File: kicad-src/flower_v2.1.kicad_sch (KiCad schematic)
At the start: 24 parts, among them J1 Conn_01x05_Male, J2 Capacitance PCB sensor, Q1 BSS84, SW1 SW_Push, SW2 SW_Push, U1 E18-MS1-PCB, U2 HSU-CHM-01A, U3 DS18B20U

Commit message: Update PCB layout
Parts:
- gave numbers to parts that had none: 1
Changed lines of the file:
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@@
   (symbol (lib_id "Device:C") (at 242.57 137.16 0) (unit 1)
     (in_bom yes) (on_board yes) (fields_autoplaced)
-    (property "Reference" "C?" (id 0) (at 246.38 135.8899 0)
+    (property "Reference" "C6" (id 0) (at 246.38 135.8899 0)
       (effects (font (size 1.27 1.27)) (justify left))
     )
@@
   (symbol (lib_id "Graphic:Logo_Open_Hardware_Small") (at 276.86 175.26 0) (unit 1)
     (in_bom yes) (on_board yes) (fields_autoplaced)
-    (property "Reference" "#LOGO?" (id 0) (at 276.86 168.275 0)
+    (property "Reference" "#LOGO1" (id 0) (at 276.86 168.275 0)
       (effects (font (size 1.27 1.27)) hide)
     )
@@
   (symbol_instances
     (path "/13f92a83-1550-43ad-ac23-b0e99ea3e589"
-      (reference "#LOGO?") (unit 1) (value "Logo_Open_Hardware_Small") (footprint "")
+      (reference "#LOGO1") (unit 1) (value "Logo_Open_Hardware_Small") (footprint "")
     )
     (path "/2f47706e-deb1-47a3-ad7d-bf0831227ea1"
@@
     )
     (path "/1078c351-8d03-4a20-b476-db003f88e220"
-      (reference "C?") (unit 1) (value "100nF") (footprint "Capacitor_SMD:C_0402_1005Metric")
+      (reference "C6") (unit 1) (value "100nF") (footprint "Capacitor_SMD:C_0402_1005Metric")
     )
     (path "/fd96ccba-4af7-423d-a91a-5897f7f71caa"

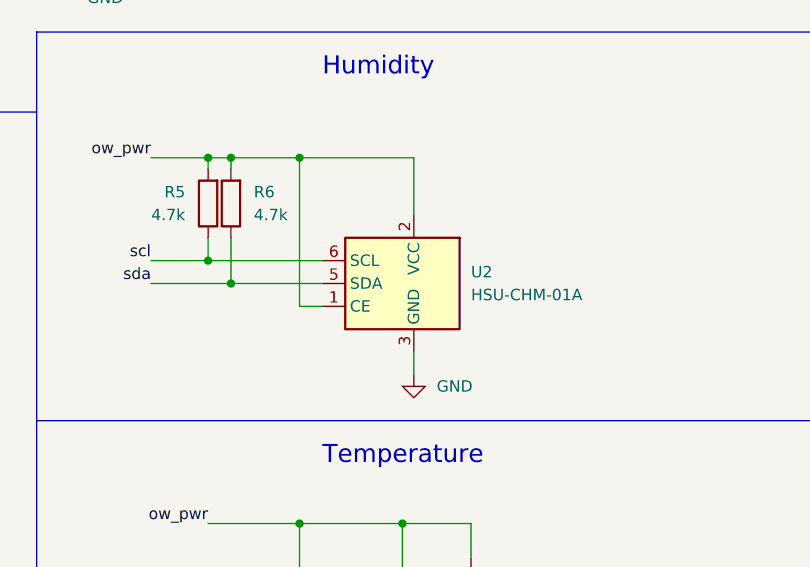
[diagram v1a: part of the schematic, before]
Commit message: hw2.1a: Fix HSU-CHM footprint
Fixes #1
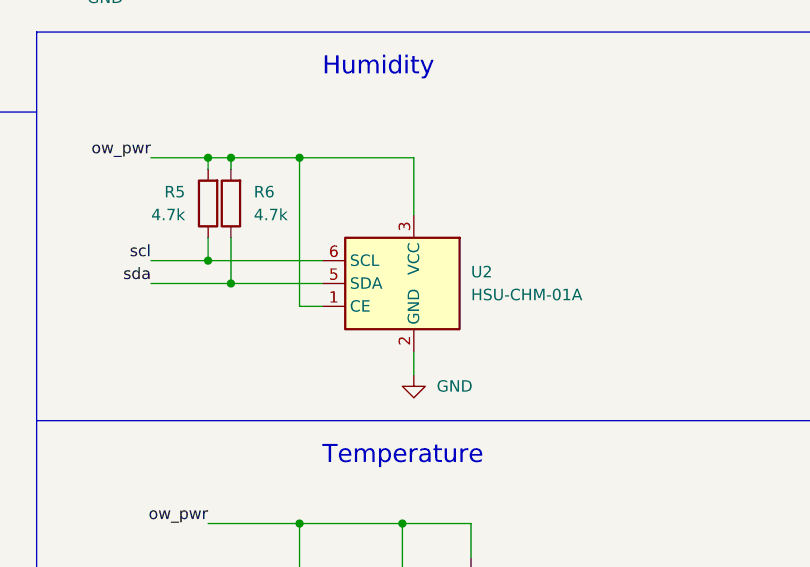
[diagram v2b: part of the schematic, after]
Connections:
- net GND: now also U2.2 (GND); no longer U2.3 (NC)
- net ow_pwr: now also U2.3 (VCC); no longer U2.2 (VCC)
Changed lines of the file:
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@@
     (title "flower mon")
     (date "2022-05-24")
-    (rev "r2.1")
+    (rev "r2.1a")
     (company "Greg Davill <greg.davill@gmail.com>")
     (comment 2 "OSHW: GPL-3.0")
@@
     (pin "2")
     (pin "3")
-    (pin "3")
     (pin "4")

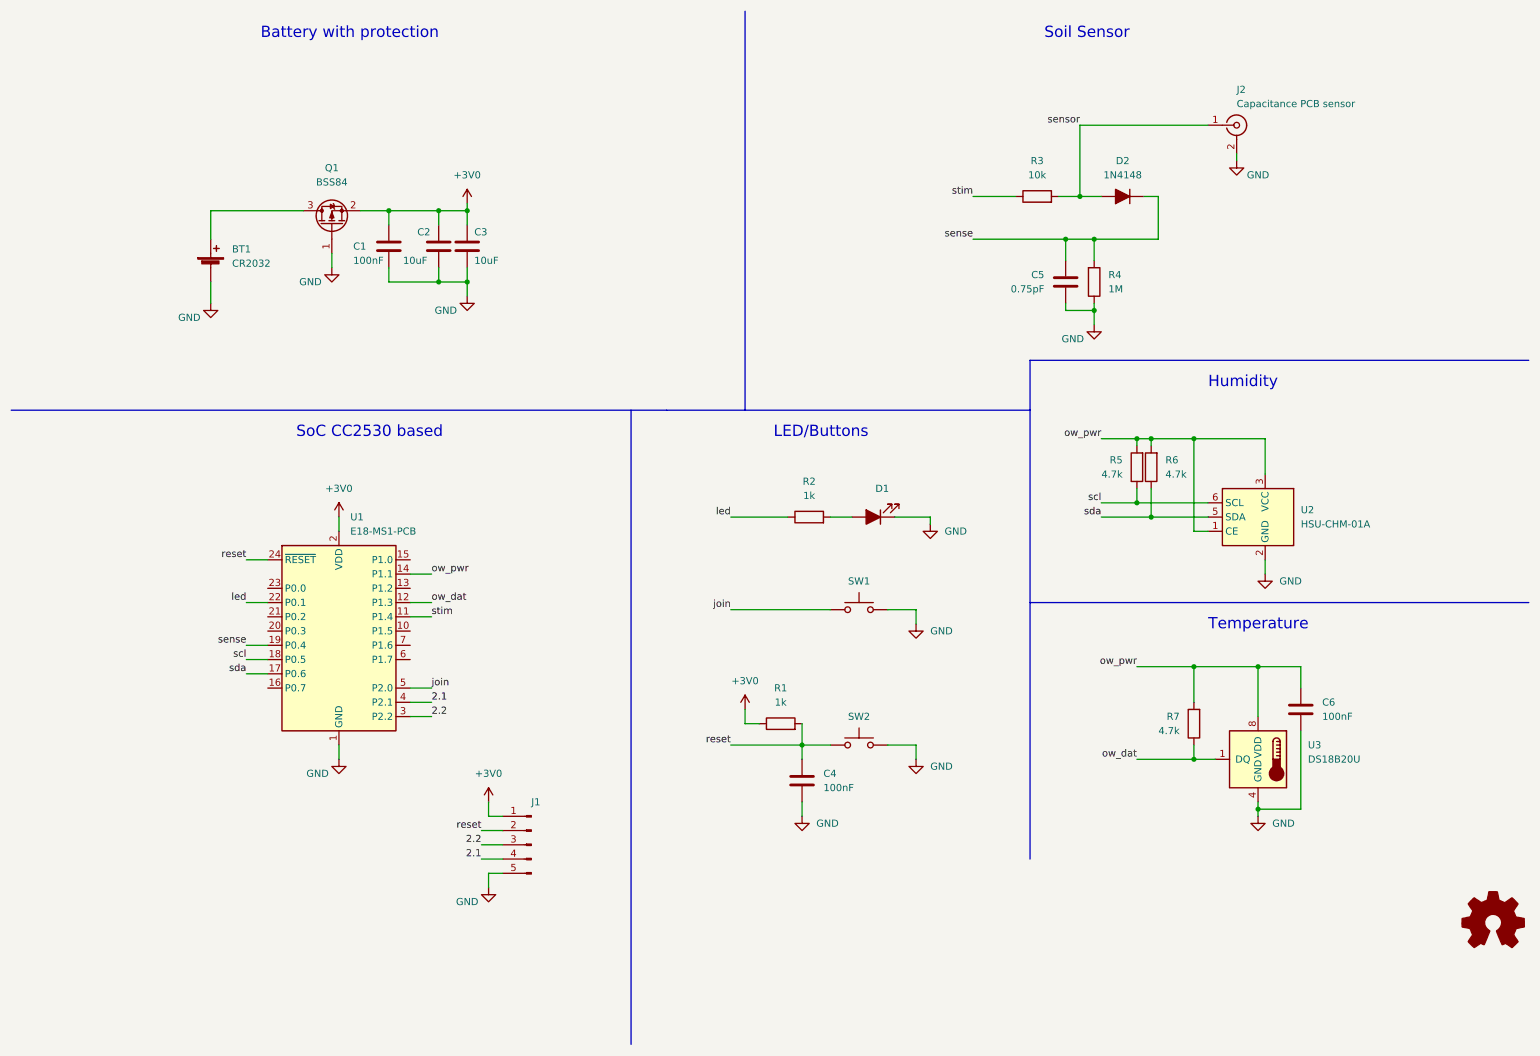
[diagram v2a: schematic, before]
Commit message: hw2.1a: Fix bugs
- Added 220uF Tantulum cap, fixes #2
- Removed DS18B20, fixes #3
- Updated battery footprint, fixes #4
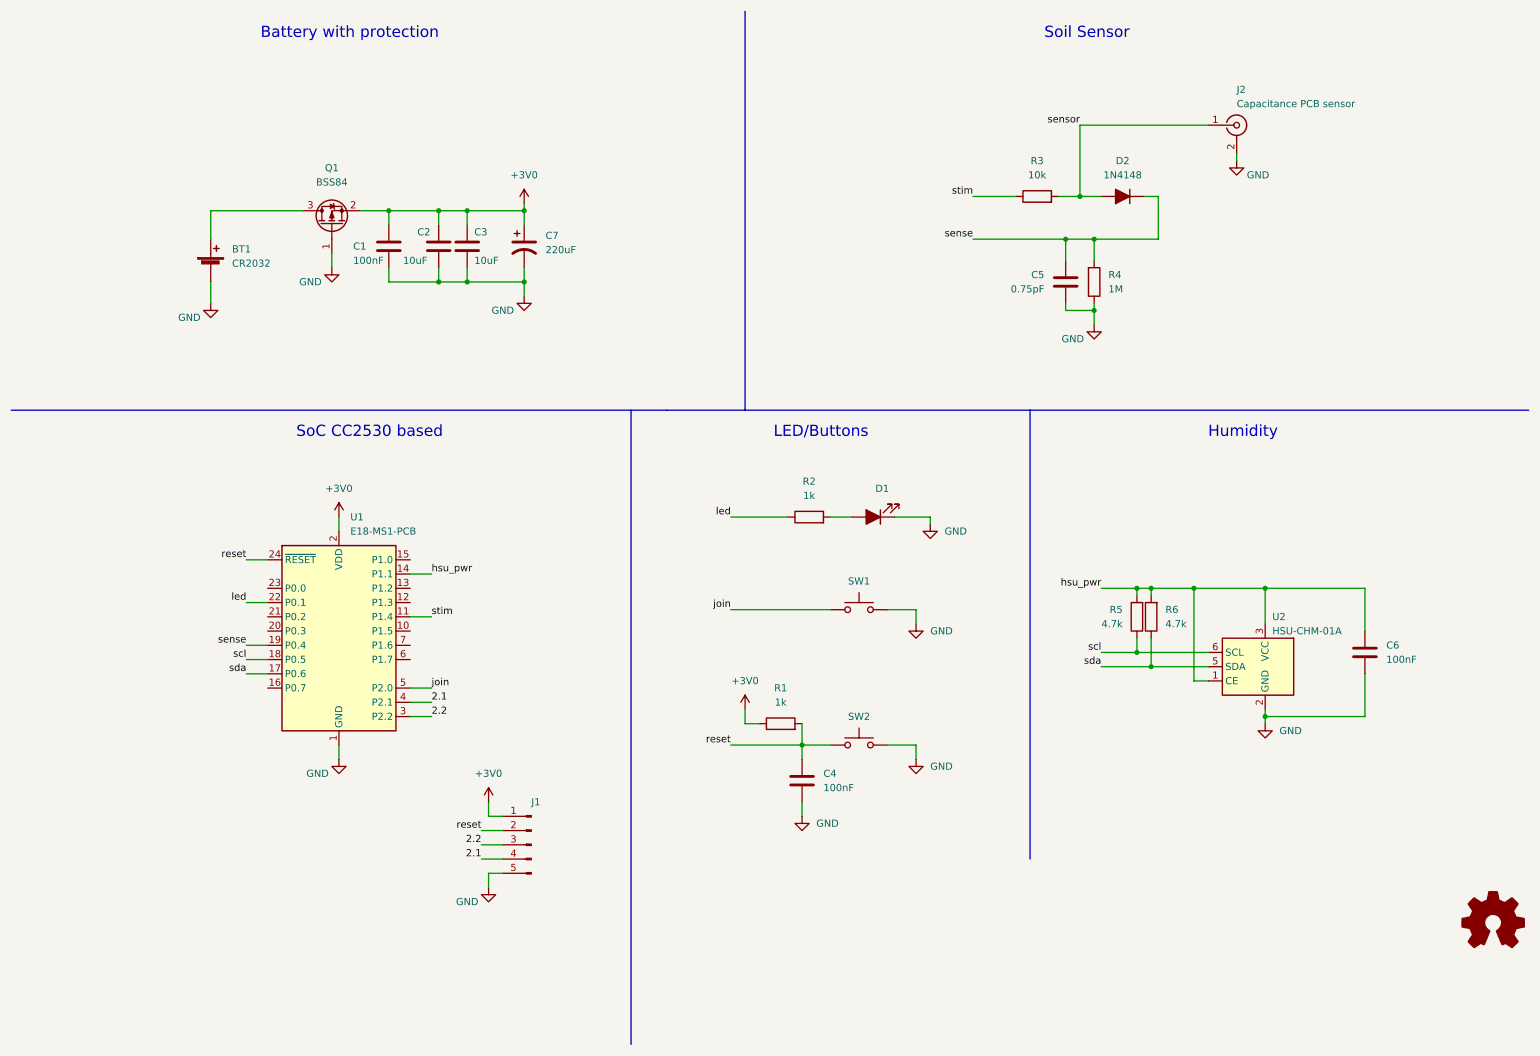
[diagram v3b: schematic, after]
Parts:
- removed R7: 4.7k, Resistor_SMD:R_0402_1005Metric, symbol Device:R
- removed U3: DS18B20U, Package_SO:MSOP-8_3x3mm_P0.65mm, symbol Sensor_Temperature:DS18B20U
- added C7: 220uF, Capacitor_Tantalum_SMD:CP_EIA-3528-21_Kemet-B, symbol Device:C_Polarized_US
- BT1: footprint Battery:BatteryHolder_LINX_BAT-HLD-012-SMT -> lib:keystone_1058
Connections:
- net +3V0: now also C7.1
- net GND: now also C7.2
- net ow_dat: no longer names the net of U1.12 (P1.3)
- net ow_pwr renamed hsu_pwr
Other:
- note removed: "Temperature"
- moved on the sheet: C6, R5, R6, U2
